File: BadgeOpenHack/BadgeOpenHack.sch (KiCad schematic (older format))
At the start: 23 parts, among them J1 Conn_01x04_Male, J2 USB_B_Micro, U1 ATSAMD11C14A-SS, U2 AP2112K-3.3TRG1

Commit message: Update schematics change footprints and floorplan
TODO:
- Change SAMD11 to LEDs pins
- Add reset button
- Add action button
- add hole for lanyard
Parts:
- removed R1, R2, R3, R4, R5, R6, R7, R8: 180, Resistor_SMD:R_0805_2012Metric_Pad1.15x1.40mm_HandSolder, symbol Device:R_Small
- removed U2: AP2112K-3.3TRG1, SOT95P285X140-5N, symbol electroniccats:AP2112K-3.3TRG1
- added C2, C3: 10uF, Capacitor_SMD:C_0805_2012Metric_Pad1.15x1.40mm_HandSolder, symbol Device:C
- added RN1, RN2: R_Pack04, Resistor_SMD:R_Array_Convex_4x0603, symbol Device:R_Pack04
- added U2: AP2112K-3.3, Package_TO_SOT_SMD:SOT-23-5, symbol Regulator_Linear:AP2112K-3.3
- BT1: manf# (none) -> BAT-HLD-012-SMT
- C1: manf# (none) -> 885012207072
- D1, D2, D3, D4, D5, D6, D7: value LED -> R_LED; footprint LED_SMD:LED_0805_2012Metric_Pad1.15x1.40mm_HandSolder -> BadgeOpenHack:LYT77K-K2M1-NoHole; manf# (none) -> LY T776-R1S2-26-Z
- D8: renamed from D9; value LED -> R_LED; footprint LED_SMD:LED_0805_2012Metric_Pad1.15x1.40mm_HandSolder -> BadgeOpenHack:LYT77K-K2M1-NoHole; manf# (none) -> LY T776-R1S2-26-Z
- D9: renamed from D8; footprint Diode_THT:D_DO-201AD_P15.24mm_Horizontal -> Diode_SMD:D_SOD-123F; manf# (none) -> MBR120VLSFT3G
- J2: manf# (none) -> 629105150521
- U1: symbol MCU_Microchip_SAMD:ATSAMD11C14A-SS -> BadgeOpenHack-rescue:ATSAMD11C14A-SS-MCU_Microchip_SAMD; manf# (none) -> ATSAMD11C14A-SSUT
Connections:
- net +3V3: now also D9.1 (K)
- net GND: now also C2.2, C3.2, RN1.5 (R4.2), RN1.6 (R3.2), RN1.7 (R2.2), RN1.8 (R1.2), RN2.5 (R4.2), RN2.6 (R3.2), RN2.7 (R2.2), RN2.8 (R1.2), U2.2 (GND)
- net VCC: now also C2.1, U2.1 (VIN), U2.3 (EN)
- net at D1.1 (K): now also RN1.1 (R1.1)
- net at D9.2 (A): now also C3.1, U2.5 (VOUT)
- net at D2.1 (K): now also RN1.2 (R2.1)
- net at D3.1 (K): now also RN1.3 (R3.1)
- net at D4.1 (K): now also RN1.4 (R4.1)
- net at D5.1 (K): now also RN2.1 (R1.1)
- net at D6.1 (K): now also RN2.2 (R2.1)
- net at D7.1 (K): now also RN2.3 (R3.1)
- net at D8.1 (K): now also RN2.4 (R4.1)
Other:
- moved on the sheet: D1, D2, D3, D4, D5, D6, D7, D8, D9

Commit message: Update LED arrange almost route
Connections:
- net D0: now also U1.5 (PA15); no longer U1.2 (PA08/XIN)
- net D1: now also U1.4 (PA14); no longer U1.3 (PA09/XOUT)
- net D2: now also U1.3 (PA09/XOUT); no longer U1.13 (PA02)
- net D3: now also U1.2 (PA08/XIN); no longer U1.14 (PA04)
- net D5: now also U1.14 (PA04); no longer U1.4 (PA14)
- net D6: now also U1.13 (PA02); no longer U1.5 (PA15)
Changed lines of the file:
@@
 Text Label 4640 3340 2    50   ~ 0
 SWDIO
-Text Label 4640 3540 0    50   ~ 0
+Text Label 5950 3440 0    50   ~ 0
 D0
-Text Label 4640 3640 0    50   ~ 0
+Text Label 5940 3340 0    50   ~ 0
 D1
-Text Label 5940 3040 0    50   ~ 0
+Text Label 4640 3640 2    50   ~ 0
 D2
-Text Label 5940 3140 0    50   ~ 0
+Text Label 4640 3540 2    50   ~ 0
 D3
 Text Label 5940 3240 0    50   ~ 0
 D4
-Text Label 5940 3340 0    50   ~ 0
+Text Label 5940 3140 0    50   ~ 0
 D5
-Text Label 5950 3440 0    50   ~ 0
+Text Label 5940 3040 0    50   ~ 0
 D6
 $Comp
@@
 U 1 1 5D76B49B
 P 8745 3845
-F 0 "RN2" V 8328 3845 50  0000 C CNN
-F 1 "R_Pack04" V 8419 3845 50  0000 C CNN
+F 0 "RN2" V 9035 3850 50  0000 C CNN
+F 1 "R_Pack04" V 8945 3850 50  0000 C CNN
 F 2 "Resistor_SMD:R_Array_Convex_4x0603" V 9020 3845 50  0001 C CNN
 F 3 "~" H 8745 3845 50  0001 C CNN

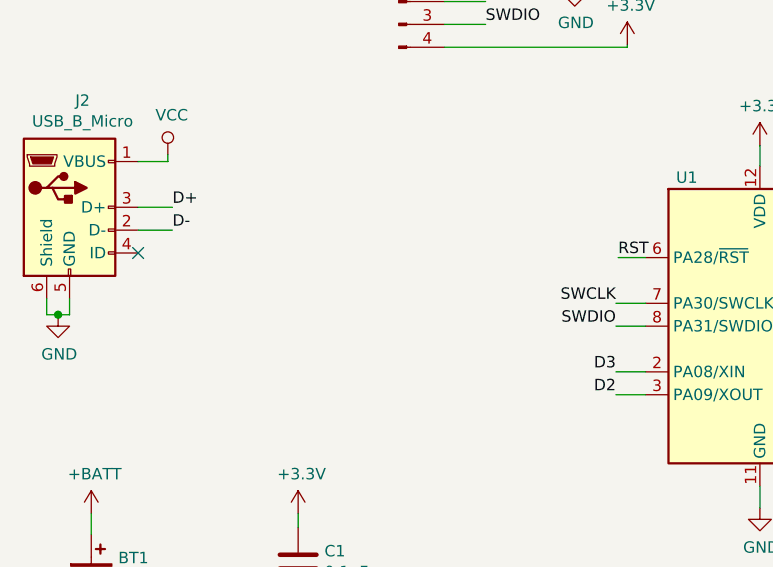
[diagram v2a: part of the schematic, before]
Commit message: add rst button complete route
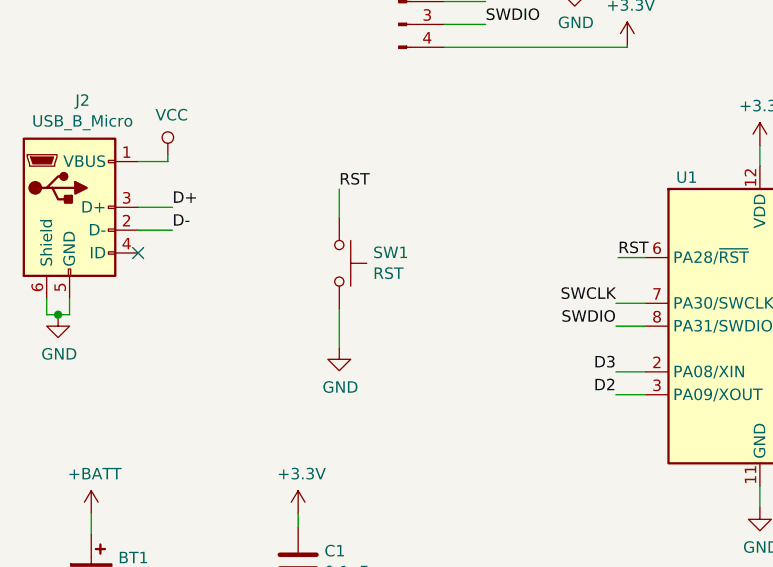
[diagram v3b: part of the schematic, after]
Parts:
- added SW1: RST, Button_Switch_SMD:SW_SPST_TL3342, symbol Switch:SW_Push
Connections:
- net GND: now also SW1.2
- net RST: now also SW1.1
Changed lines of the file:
@@
 Wire Wire Line
 	9180 3345 9180 3445
+$Comp
+L Switch:SW_Push SW1
+U 1 1 5D73E48F
+P 3430 3065
+F 0 "SW1" V 3384 3213 50  0000 L CNN
+F 1 "RST" V 3475 3213 50  0000 L CNN
+F 2 "Button_Switch_SMD:SW_SPST_TL3342" H 3430 3265 50  0001 C CNN
+F 3 "~" H 3430 3265 50  0001 C CNN
+	1    3430 3065
+	0    1    1    0
+$EndComp
+Text Label 3430 2740 0    50   ~ 0
+RST
+Wire Wire Line
+	3430 2740 3430 2865
+$Comp
+L power:GND #PWR?
+U 1 1 5D7412B1
+P 3430 3435
+F 0 "#PWR?" H 3430 3185 50  0001 C CNN
+F 1 "GND" H 3435 3262 50  0000 C CNN
+F 2 "" H 3430 3435 50  0001 C CNN
+F 3 "" H 3430 3435 50  0001 C CNN
+	1    3430 3435
+	1    0    0    -1
+$EndComp
+Wire Wire Line
+	3430 3435 3430 3265
 $EndSCHEMATC
